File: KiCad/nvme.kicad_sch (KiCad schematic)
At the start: 40 parts, among them J10 Bus_M.2_Socket_M, J11 Bus_M.2_Socket_M, J12 Bus_M.2_Socket_M, J13 Bus_M.2_Socket_M, J14 Bus_M.2_Socket_M

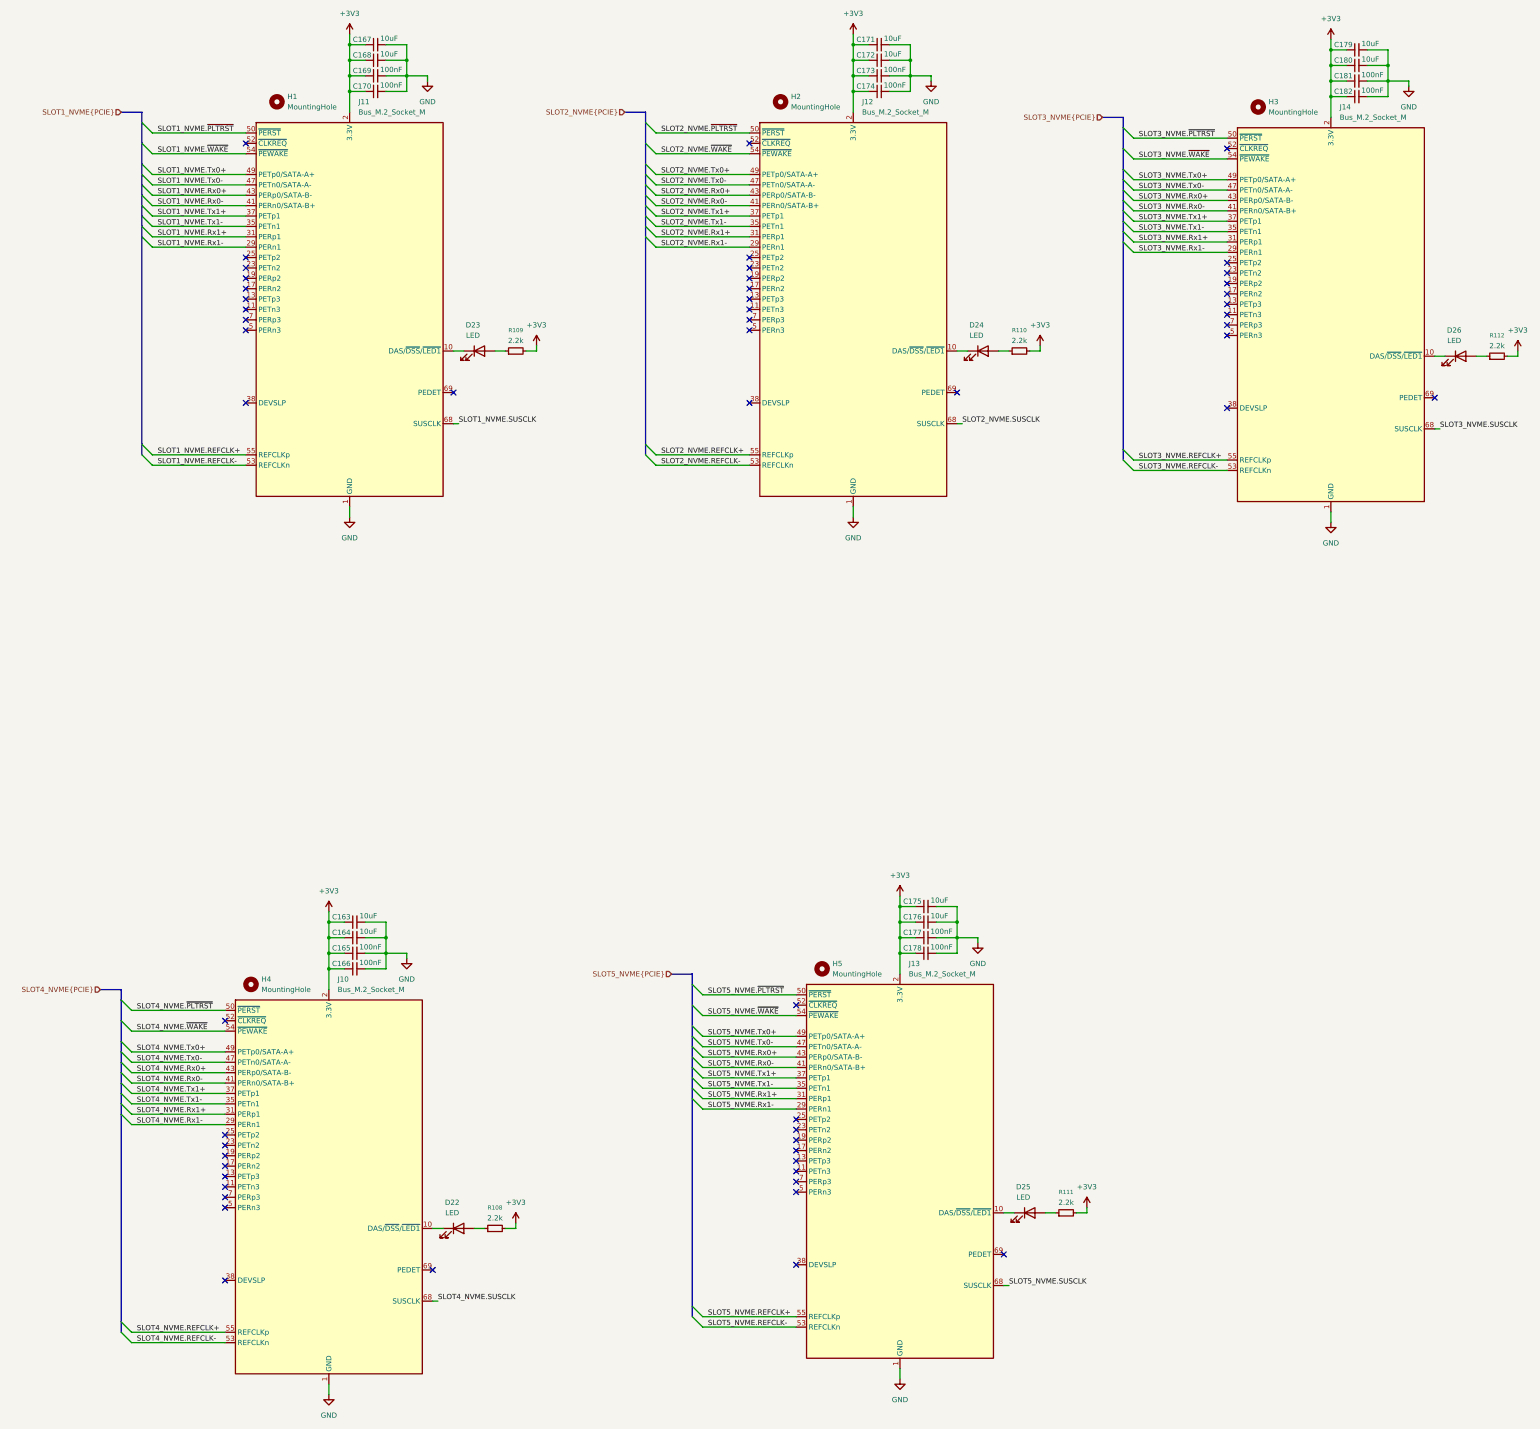
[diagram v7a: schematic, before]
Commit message: Finish fixing footprints
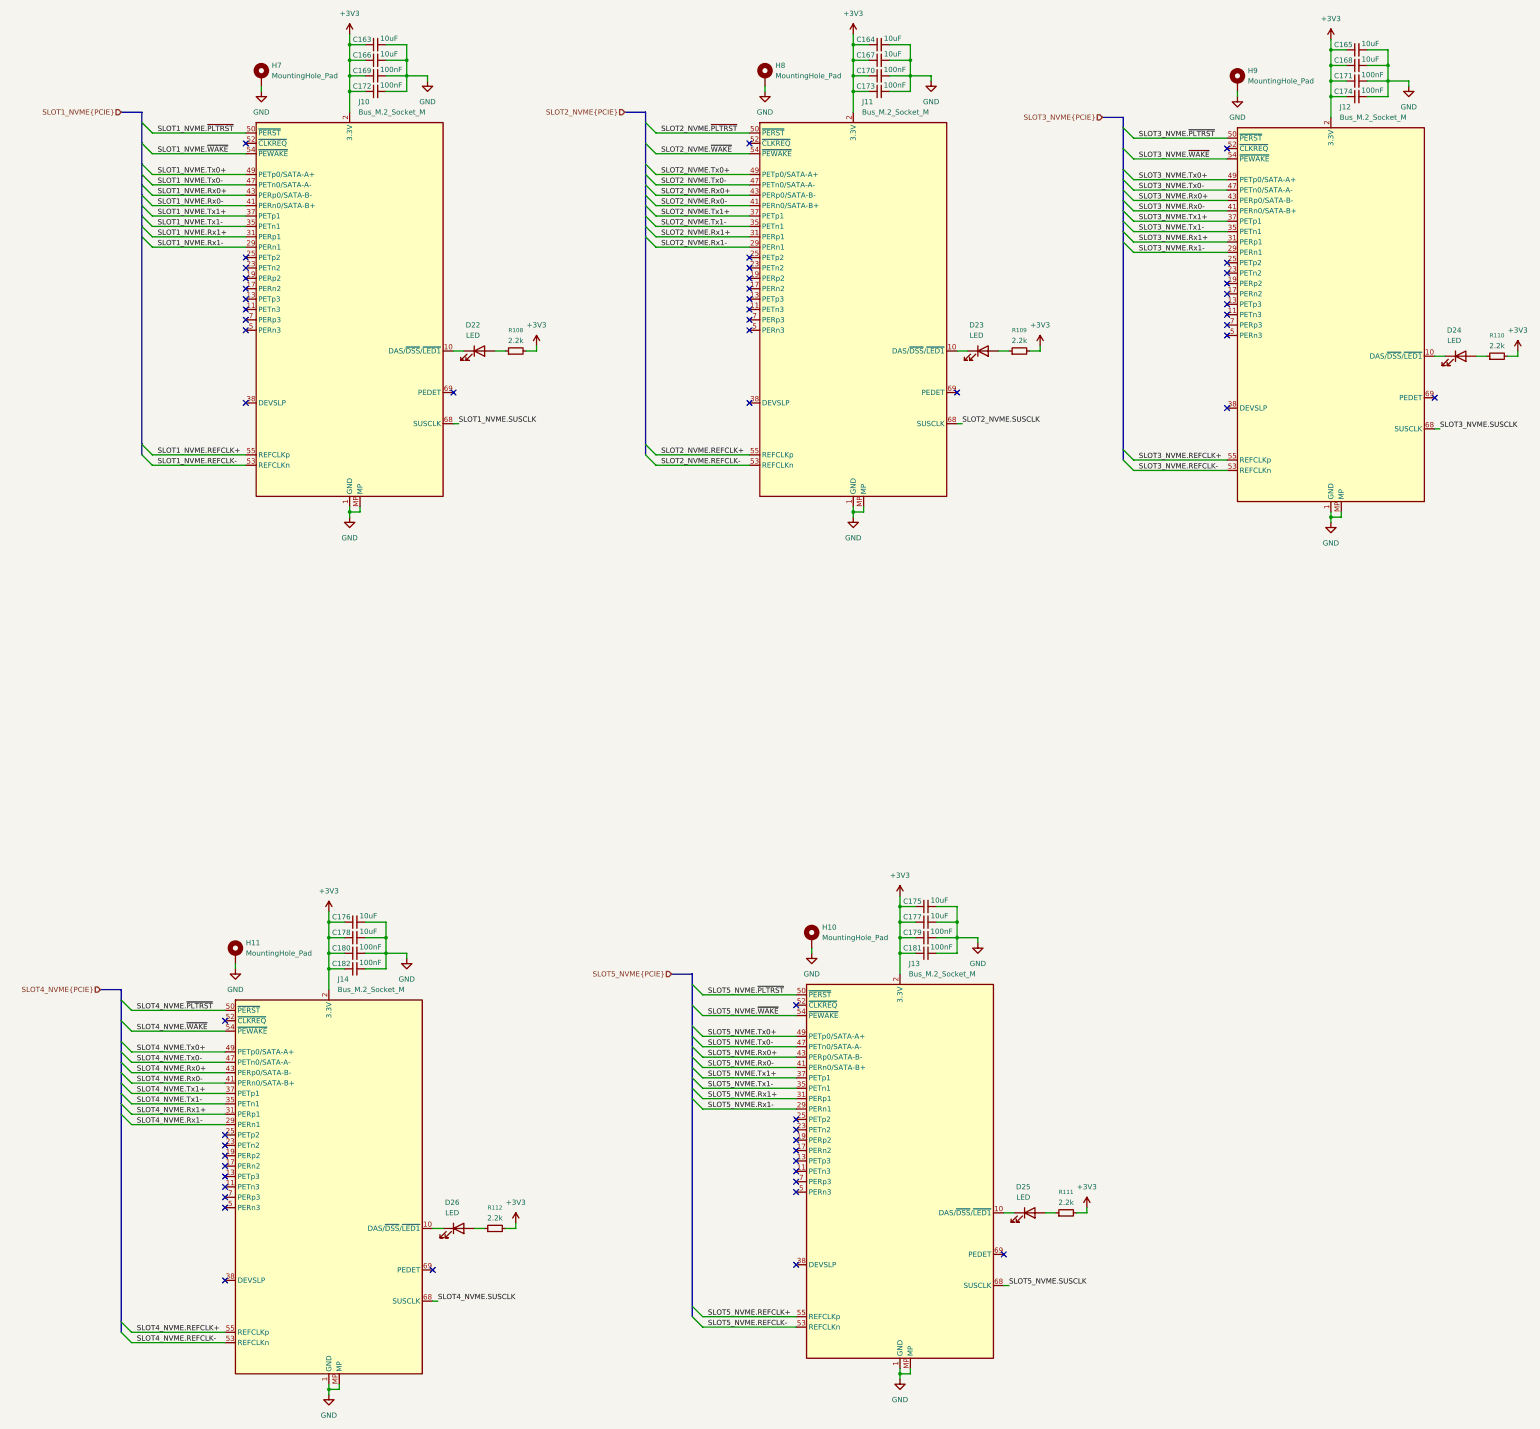
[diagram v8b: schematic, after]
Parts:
- removed H1, H2, H3, H4, H5: MountingHole, symbol Mechanical:MountingHole
- removed J10: Bus_M.2_Socket_M, EasyEDA2KiCAD:CONN-SMD_AS0BC21-S30BM-7H, symbol Connector:Bus_M.2_Socket_M
- added H10, H11, H7, H8, H9: MountingHole_Pad, MountingHole:MountingHole_2.2mm_M2_Pad_Via, symbol Mechanical:MountingHole_Pad
- added J11: Bus_M.2_Socket_M, EasyEDA2KiCAD:CONN-SMD_AS0BC21-S30BM-7H, symbol Connector:Bus_M.2_Socket_M
- renumbered C167 to C163, C171 to C164, C179 to C165, C168 to C166, C172 to C167, C180 to C168, C173 to C170, C181 to C171, C170 to C172, C174 to C173, C182 to C174, C163 to C176, C176 to C177, C164 to C178, C177 to C179, C165 to C180, C178 to C181, C166 to C182, D23 to D22, D24 to D23, D26 to D24, D22 to D26, J11 to J10, R109 to R108, R110 to R109, R112 to R110, R108 to R112
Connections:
- net +3V3: now also J11.12 (3.3V), J11.14 (3.3V), J11.16 (3.3V), J11.18 (3.3V), J11.2 (3.3V), J11.4 (3.3V), J11.70 (3.3V), J11.72 (3.3V), J11.74 (3.3V)
- net GND: now also J10.MP, J12.MP, J13.MP, J14.MP, H10.1, H11.1, H7.1, H8.1, H9.1, J11.1 (GND), J11.15 (GND), J11.21 (GND), J11.27 (GND), J11.3 (GND), J11.33 (GND), J11.39 (GND), J11.45 (GND), J11.51 (GND), J11.57 (GND), J11.71 (GND), J11.73 (GND), J11.75 (GND), J11.9 (GND), J11.MP
- net SLOT2_NVME.REFCLK+: now also J11.55 (REFCLKp); no longer J12.55 (REFCLKp)
- net SLOT2_NVME.REFCLK-: now also J11.53 (REFCLKn); no longer J12.53 (REFCLKn)
- net SLOT2_NVME.Rx0+: now also J11.43 (PERp0/SATA-B-); no longer J12.43 (PERp0/SATA-B-)
- net SLOT2_NVME.Rx0-: now also J11.41 (PERn0/SATA-B+); no longer J12.41 (PERn0/SATA-B+)
- net SLOT2_NVME.Rx1+: now also J11.31 (PERp1); no longer J12.31 (PERp1)
- net SLOT2_NVME.Rx1-: now also J11.29 (PERn1); no longer J12.29 (PERn1)
- net SLOT2_NVME.SUSCLK: now also J11.68 (SUSCLK); no longer J12.68 (SUSCLK)
- net SLOT2_NVME.Tx0+: now also J11.49 (PETp0/SATA-A+); no longer J12.49 (PETp0/SATA-A+)
- net SLOT2_NVME.Tx0-: now also J11.47 (PETn0/SATA-A-); no longer J12.47 (PETn0/SATA-A-)
- net SLOT2_NVME.Tx1+: now also J11.37 (PETp1); no longer J12.37 (PETp1)
- net SLOT2_NVME.Tx1-: now also J11.35 (PETn1); no longer J12.35 (PETn1)
- net SLOT2_NVME.~{PLTRST}: now also J11.50 (~{PERST}); no longer J12.50 (~{PERST})
- net SLOT2_NVME.~{WAKE}: now also J11.54 (~{PEWAKE}); no longer J12.54 (~{PEWAKE})
- net SLOT3_NVME.REFCLK+: now also J12.55 (REFCLKp); no longer J14.55 (REFCLKp)
- net SLOT3_NVME.REFCLK-: now also J12.53 (REFCLKn); no longer J14.53 (REFCLKn)
- net SLOT3_NVME.Rx0+: now also J12.43 (PERp0/SATA-B-); no longer J14.43 (PERp0/SATA-B-)
- net SLOT3_NVME.Rx0-: now also J12.41 (PERn0/SATA-B+); no longer J14.41 (PERn0/SATA-B+)
- net SLOT3_NVME.Rx1+: now also J12.31 (PERp1); no longer J14.31 (PERp1)
- net SLOT3_NVME.Rx1-: now also J12.29 (PERn1); no longer J14.29 (PERn1)
- net SLOT3_NVME.SUSCLK: now also J12.68 (SUSCLK); no longer J14.68 (SUSCLK)
- net SLOT3_NVME.Tx0+: now also J12.49 (PETp0/SATA-A+); no longer J14.49 (PETp0/SATA-A+)
- net SLOT3_NVME.Tx0-: now also J12.47 (PETn0/SATA-A-); no longer J14.47 (PETn0/SATA-A-)
- net SLOT3_NVME.Tx1+: now also J12.37 (PETp1); no longer J14.37 (PETp1)
- net SLOT3_NVME.Tx1-: now also J12.35 (PETn1); no longer J14.35 (PETn1)
- net SLOT3_NVME.~{PLTRST}: now also J12.50 (~{PERST}); no longer J14.50 (~{PERST})
- net SLOT3_NVME.~{WAKE}: now also J12.54 (~{PEWAKE}); no longer J14.54 (~{PEWAKE})
- net SLOT4_NVME.REFCLK+: now also J14.55 (REFCLKp)
- net SLOT4_NVME.REFCLK-: now also J14.53 (REFCLKn)
- net SLOT4_NVME.Rx0+: now also J14.43 (PERp0/SATA-B-)
- net SLOT4_NVME.Rx0-: now also J14.41 (PERn0/SATA-B+)
- net SLOT4_NVME.Rx1+: now also J14.31 (PERp1)
- net SLOT4_NVME.Rx1-: now also J14.29 (PERn1)
- net SLOT4_NVME.SUSCLK: now also J14.68 (SUSCLK)
- net SLOT4_NVME.Tx0+: now also J14.49 (PETp0/SATA-A+)
- net SLOT4_NVME.Tx0-: now also J14.47 (PETn0/SATA-A-)
- net SLOT4_NVME.Tx1+: now also J14.37 (PETp1)
- net SLOT4_NVME.Tx1-: now also J14.35 (PETn1)
- net SLOT4_NVME.~{PLTRST}: now also J14.50 (~{PERST})
- net SLOT4_NVME.~{WAKE}: now also J14.54 (~{PEWAKE})
- net at D24.1 (K): now also J12.10 (DAS/~{DSS}/~{LED1}); no longer J14.10 (DAS/~{DSS}/~{LED1})
- net at D26.1 (K): now also J14.10 (DAS/~{DSS}/~{LED1})
- net at D23.1 (K): now also J11.10 (DAS/~{DSS}/~{LED1}); no longer J12.10 (DAS/~{DSS}/~{LED1})
